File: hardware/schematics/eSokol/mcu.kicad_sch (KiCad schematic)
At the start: 12 parts, among them J1 DB25, Q6 AO3400A, SW1 SW_KEY, U2 YAAJ_BluePill_SWD_Breakout, U3 TP4056, U5 AMS1117-5.0, U8 DS18S20

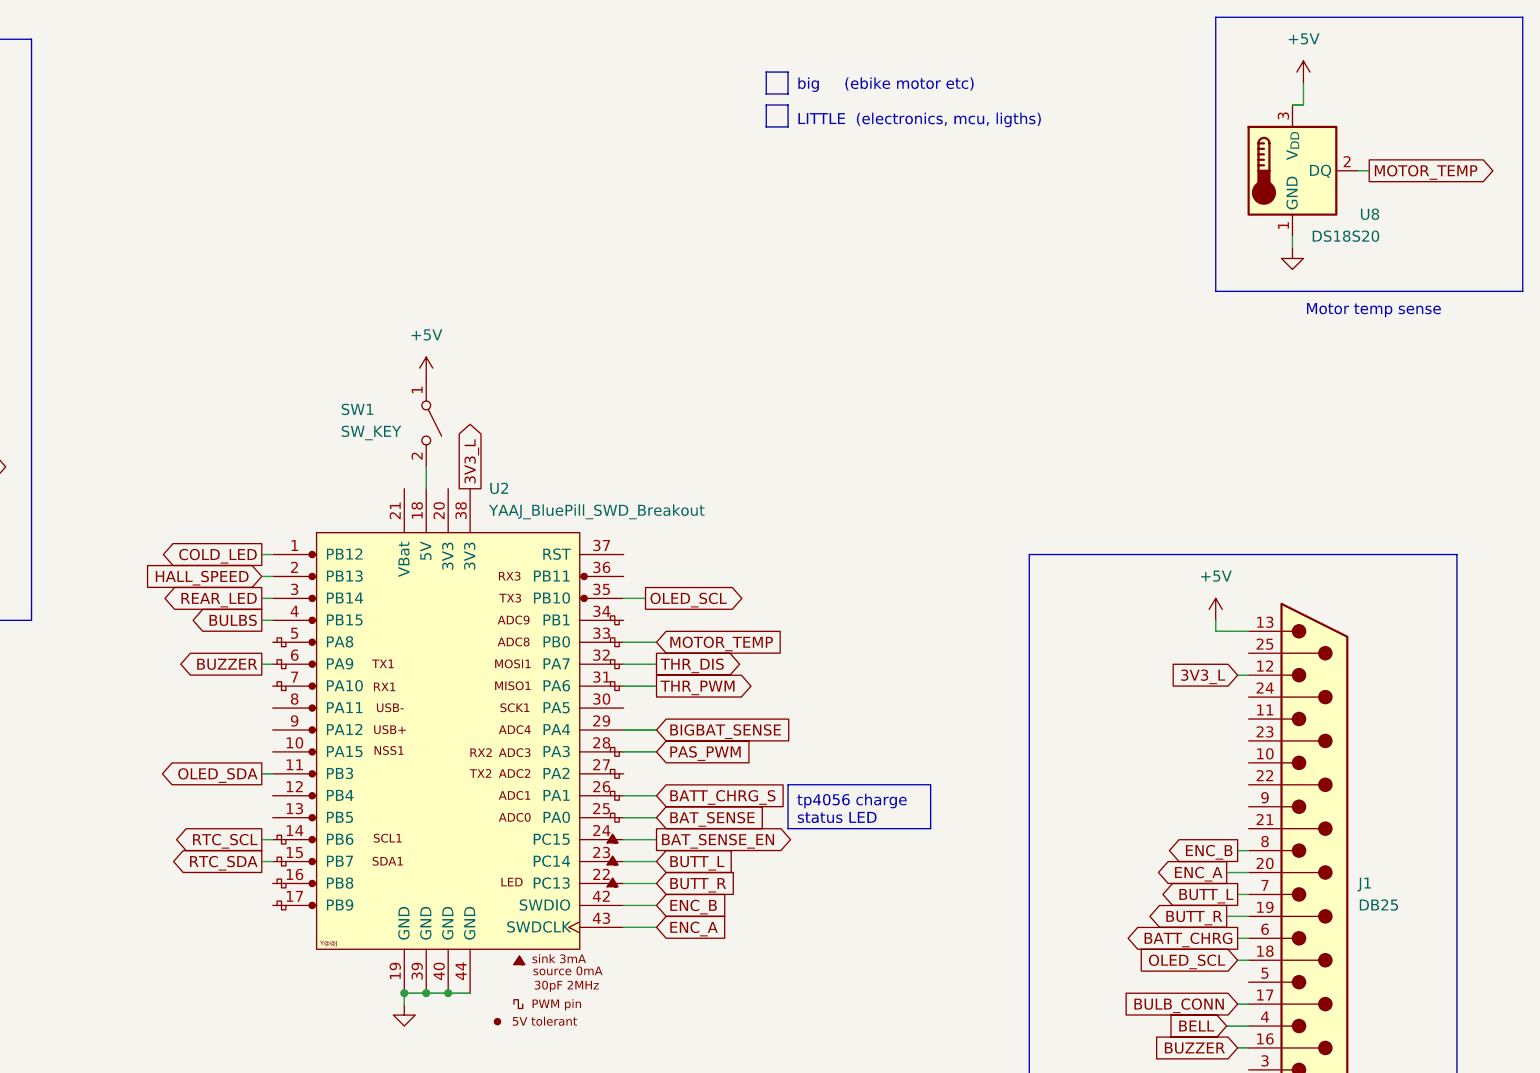
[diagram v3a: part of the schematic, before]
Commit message: Create one BIG schematic containing everything related to motor and its driver
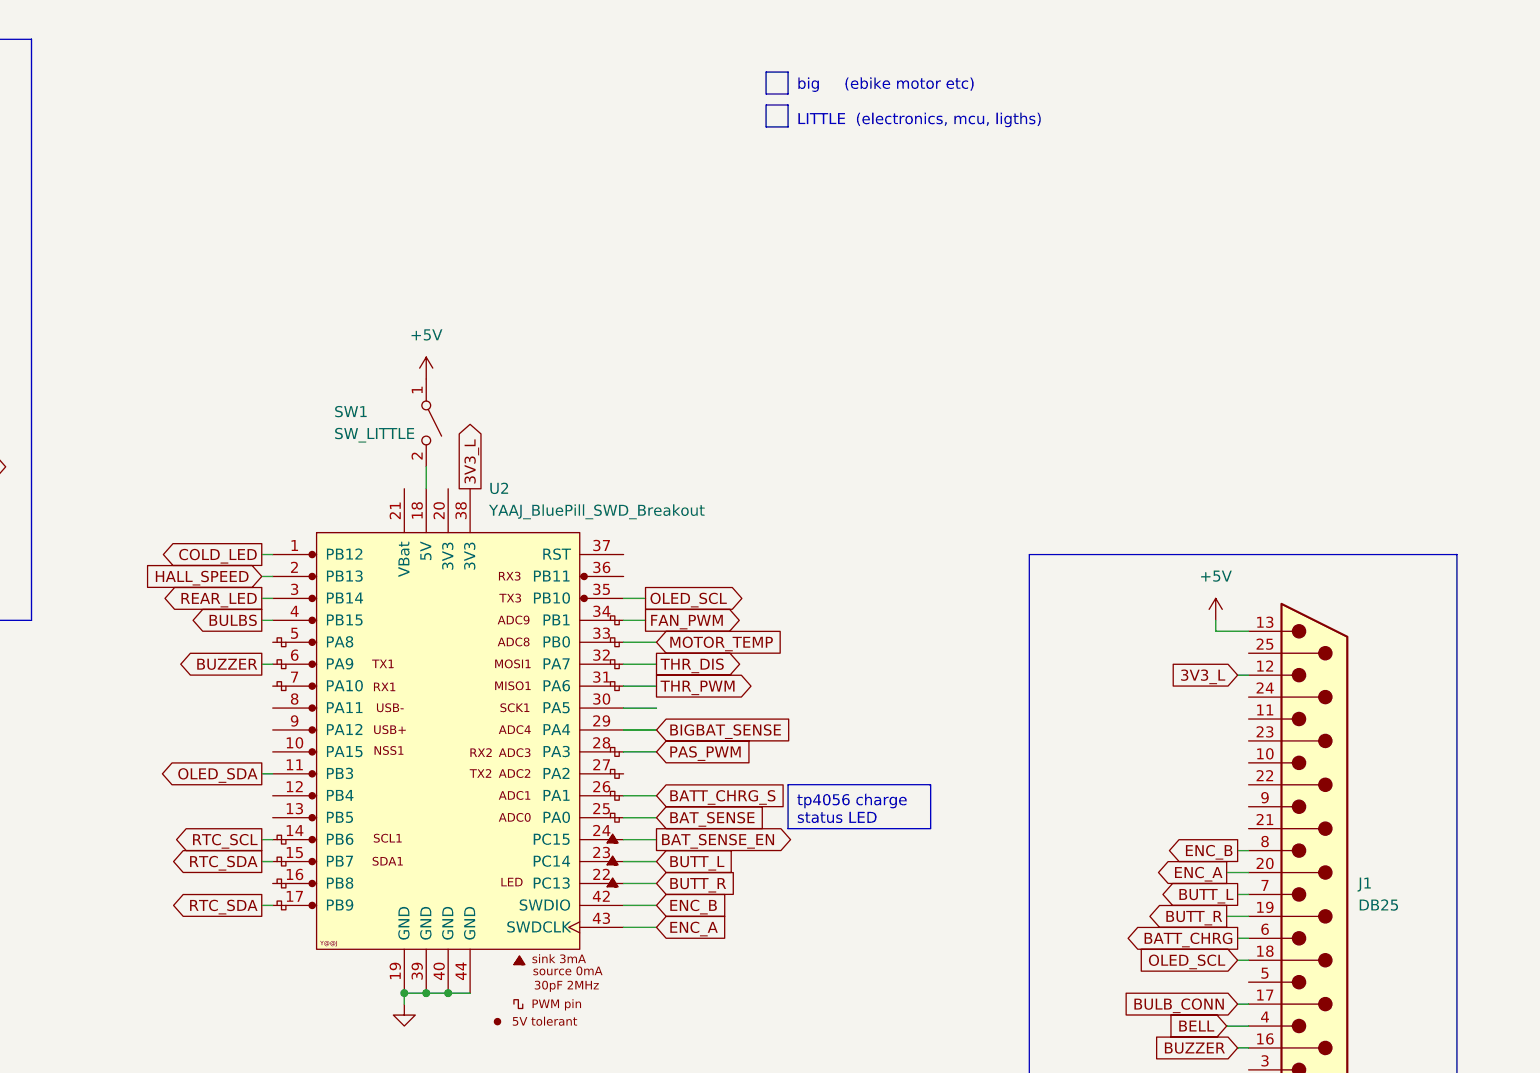
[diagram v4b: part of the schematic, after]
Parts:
- removed U8: DS18S20, Package_TO_SOT_THT:TO-92_Inline, symbol Sensor_Temperature:DS18S20
- SW1: value SW_KEY -> SW_LITTLE
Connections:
- net RTC_SDA: now also U2.17 (PB9)
- net FAN_PWM: now reaches U2.34 (PB1)
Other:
- note removed: "Motor temp sense"
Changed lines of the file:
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@@
+	(wire
+		(pts
+			(xy 177.8 93.98) (xy 181.61 93.98)
+		)
+		(stroke
+			(width 0)
+			(type default)
+		)
+	)
+	(wire
+		(pts
+			(xy 177.8 83.82) (xy 180.34 83.82)
+		)
+		(stroke
+			(width 0)
+			(type default)
+		)
+	)
 	(wire
 		(pts
@@
 	(wire
 		(pts
+			(xy 135.89 116.84) (xy 137.16 116.84)
+		)
+		(stroke
+			(width 0)
+			(type default)
+		)
+	)
+	(wire
+		(pts
 			(xy 135.89 111.76) (xy 137.16 111.76)
 		)
@@
 	(wire
 		(pts
-			(xy 256.54 21.59) (xy 256.54 24.13)
-		)
-		(stroke
-			(width 0)
-			(type default)
-		)
-	)
-	(wire
-		(pts
 			(xy 160.02 182.88) (xy 156.21 182.88)
 		)
@@
 	(wire
 		(pts
-			(xy 255.27 39.37) (xy 255.27 40.64)
-		)
-		(stroke
-			(width 0)
-			(type default)
-		)
-	)
-	(wire
-		(pts
 			(xy 137.16 81.28) (xy 135.89 81.28)
 		)
@@
 	(wire
 		(pts
-			(xy 255.27 24.13) (xy 256.54 24.13)
-		)
-		(stroke
-			(width 0)
-			(type default)
-		)
-	)
-	(wire
-		(pts
 			(xy 250.19 146.05) (xy 250.19 149.86)
 		)
@@
 		(pts
 			(xy 177.8 88.9) (xy 181.61 88.9)
-		)
-		(stroke
-			(width 0)
-			(type default)
-		)
-	)
-	(wire
-		(pts
-			(xy 264.16 31.75) (xy 262.89 31.75)
 		)
 		(stroke
@@
 			(width 0)
 			(type default)
-		)
-		(fill
-			(type none)
-		)
-	)
-	(rectangle
-		(start 246.38 13.97)
-		(end 281.94 45.72)
-		(stroke
-			(width 0)
-			(type default)
-			(color 204 102 0 1)
 		)
 		(fill
@@
 		)
 	)
-	(text "Motor temp sense\n"
-		(exclude_from_sim no)
-		(at 264.668 48.006 0)
-		(effects
-			(font
-				(size 1.27 1.27)
-				(color 204 102 0 1)
-			)
-		)
-	)
 	(text "LPT CONNECTOR (TO BIKE FRONT)"
 		(exclude_from_sim no)
@@
 		)
 	)
+	(global_label "FAN_PWM"
+		(shape output)
+		(at 180.34 83.82 0)
+		(fields_autoplaced yes)
+		(effects
+			(font
+				(size 1.27 1.27)
+				(color 204 102 0 1)
+			)
+			(justify left)
+		)
+		(property "Intersheetrefs" "${INTERSHEET_REFS}"
+			(at 191.9733 83.82 0)
+			(effects
+				(font
+					(size 1.27 1.27)
+				)
+				(justify left)
+				(hide yes)
+			)
+		)
+	)
 	(global_label "BATT_CHRG_S"
 		(shape input)
@@
 		)
 	)
-	(global_label "MOTOR_TEMP"
-		(shape output)
-		(at 264.16 31.75 0)
-		(fields_autoplaced yes)
-		(effects
-			(font
-				(size 1.27 1.27)
-				(color 204 102 0 1)
-			)
-			(justify left)
-		)
-		(property "Intersheetrefs" "${INTERSHEET_REFS}"
-			(at 279.3008 31.75 0)
-			(effects
-				(font
-					(size 1.27 1.27)
-				)
-				(justify left)
-				(hide yes)
-			)
-		)
-	)
 	(global_label "RTC_SDA"
 		(shape output)
@@
 		(property "Intersheetrefs" "${INTERSHEET_REFS}"
 			(at 238.8591 113.03 0)
+			(effects
+				(font
+					(size 1.27 1.27)
+				)
+				(justify right)
+				(hide yes)
+			)
+		)
+	)
+	(global_label "RTC_SDA"
+		(shape output)
+		(at 135.89 116.84 180)
+		(fields_autoplaced yes)
+		(effects
+			(font
+				(size 1.27 1.27)
+			)
+			(justify right)
+		)
+		(property "Intersheetrefs" "${INTERSHEET_REFS}"
+			(at 124.8615 116.84 0)
 			(effects
 				(font
@@
 	)
 	(symbol
-		(lib_id "power:+5V")
-		(at 256.54 21.59 0)
-		(unit 1)
-		(exclude_from_sim no)
-		(in_bom yes)
-		(on_board yes)
-		(dnp no)
-		(fields_autoplaced yes)
-		(property "Reference" "#PWR062"
-			(at 256.54 25.4 0)
-			(effects
-				(font
-					(size 1.27 1.27)
-				)
-				(hide yes)
-			)
-		)
-		(property "Value" "+5V"
-			(at 256.54 16.51 0)
-			(effects
-				(font
-					(size 1.27 1.27)
-				)
-			)
-		)
-		(property "Footprint" ""
-			(at 256.54 21.59 0)
-			(effects
-				(font
-					(size 1.27 1.27)
-				)
-				(hide yes)
-			)
-		)
-		(property "Datasheet" ""
-			(at 256.54 21.59 0)
-			(effects
-				(font
-					(size 1.27 1.27)
-				)
-				(hide yes)
-			)
-		)
-		(property "Description" "Power symbol creates a global label with name \"+5V\""
-			(at 256.54 21.59 0)
-			(effects
-				(font
-					(size 1.27 1.27)
-				)
-				(hide yes)
-			)
-		)
-		(pin "1"
-		)
-		(instances
-			(project "eSokol"
-				(path "/44b9e6ec-08e4-4361-b4b8-e7c9cf0a26a7/f565501d-a817-4ef9-831d-033eb352bbe6"
-					(reference "#PWR062")
-					(unit 1)
-				)
-			)
-		)
-	)
-	(symbol
 		(lib_id "power:+BATT")
 		(at 26.67 64.77 90)
@@
 		(dnp no)
 		(property "Reference" "SW1"
-			(at 145.034 59.436 90)
-			(effects
-				(font
-					(size 1.27 1.27)
-				)
-				(justify left)
-			)
-		)
-		(property "Value" "SW_KEY"
-			(at 145.034 61.976 90)
+			(at 144.272 59.69 90)
+			(effects
+				(font
+					(size 1.27 1.27)
+				)
+				(justify left)
+			)
+		)
+		(property "Value" "SW_LITTLE"
+			(at 144.272 62.23 90)
 			(effects
 				(font
@@
 				(path "/44b9e6ec-08e4-4361-b4b8-e7c9cf0a26a7/f565501d-a817-4ef9-831d-033eb352bbe6"
 					(reference "SW1")
-					(unit 1)
-				)
-			)
-		)
-	)
-	(symbol
-		(lib_id "power:GND")
-		(at 255.27 40.64 0)
-		(unit 1)
-		(exclude_from_sim no)
-		(in_bom yes)
-		(on_board yes)
-		(dnp no)
-		(fields_autoplaced yes)
-		(property "Reference" "#PWR063"
-			(at 255.27 46.99 0)
-			(effects
-				(font
-					(size 1.27 1.27)
-				)
-				(hide yes)
-			)
-		)
-		(property "Value" "GND"
-			(at 255.27 45.72 0)
-			(effects
-				(font
-					(size 1.27 1.27)
-				)
-				(hide yes)
-			)
-		)
-		(property "Footprint" ""
-			(at 255.27 40.64 0)
-			(effects
-				(font
-					(size 1.27 1.27)
-				)
-				(hide yes)
-			)
-		)
-		(property "Datasheet" ""
-			(at 255.27 40.64 0)
-			(effects
-				(font
-					(size 1.27 1.27)
-				)
-				(hide yes)
-			)
-		)
-		(property "Description" "Power symbol creates a global label with name \"GND\" , ground"
-			(at 255.27 40.64 0)
-			(effects
-				(font
-					(size 1.27 1.27)
-				)
-				(hide yes)
-			)
-		)
-		(pin "1"
-		)
-		(instances
-			(project "eSokol"
-				(path "/44b9e6ec-08e4-4361-b4b8-e7c9cf0a26a7/f565501d-a817-4ef9-831d-033eb352bbe6"
-					(reference "#PWR063")
 					(unit 1)
 				)
@@
 					(unit 1)
 				)
-			)
-		)
-	)
-	(symbol
-		(lib_id "Sensor_Temperature:DS18S20")
-		(at 255.27 31.75 0)
-		(unit 1)
-		(exclude_from_sim no)
-		(in_bom yes)
-		(on_board yes)
-		(dnp no)
-		(property "Reference" "U8"
-			(at 265.43 36.83 0)
-			(effects
-				(font
-					(size 1.27 1.27)
-				)
-				(justify right)
-			)
-		)
-		(property "Value" "DS18S20"
-			(at 265.43 39.37 0)
-			(effects
-				(font
-					(size 1.27 1.27)
-				)
-				(justify right)
-			)
-		)
-		(property "Footprint" "Package_TO_SOT_THT:TO-92_Inline"
-			(at 229.87 38.1 0)
-			(effects
-				(font
-					(size 1.27 1.27)
-				)
-				(hide yes)
-			)
-		)
-		(property "Datasheet" "http://datasheets.maximintegrated.com/en/ds/DS18S20.pdf"
-			(at 251.46 25.4 0)
-			(effects
-				(font
-					(size 1.27 1.27)
-				)
-				(hide yes)
-			)
-		)
-		(property "Description" "High-Precision 1-Wire Digital Thermometer TO-92"
-			(at 255.27 31.75 0)
-			(effects
-				(font
-					(size 1.27 1.27)
-				)
-				(hide yes)
-			)
-		)
-		(pin "3"
-		)
-		(pin "2"
-		)
-		(pin "1"
-		)
-		(instances
-			(project ""
-				(path "/44b9e6ec-08e4-4361-b4b8-e7c9cf0a26a7/f565501d-a817-4ef9-831d-033eb352bbe6"
-					(reference "U8")
-					(unit 1)
-				)

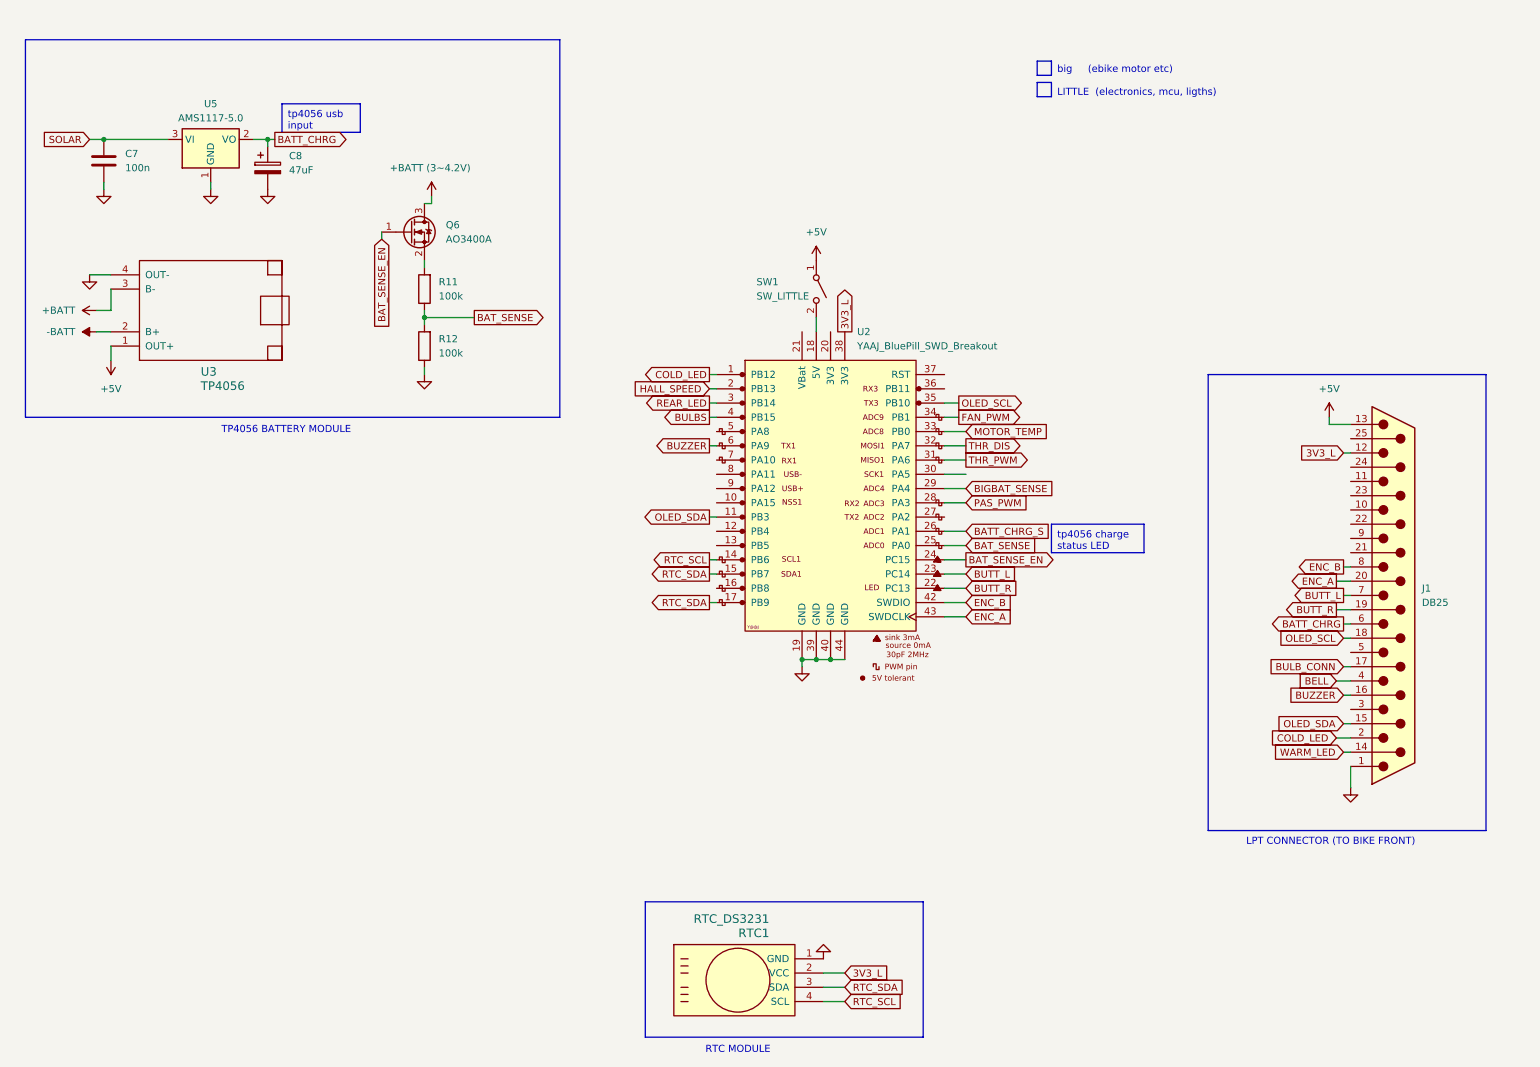
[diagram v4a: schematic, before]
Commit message: Initial TCRT5000-based rider detect, rearrange MCU pin layout
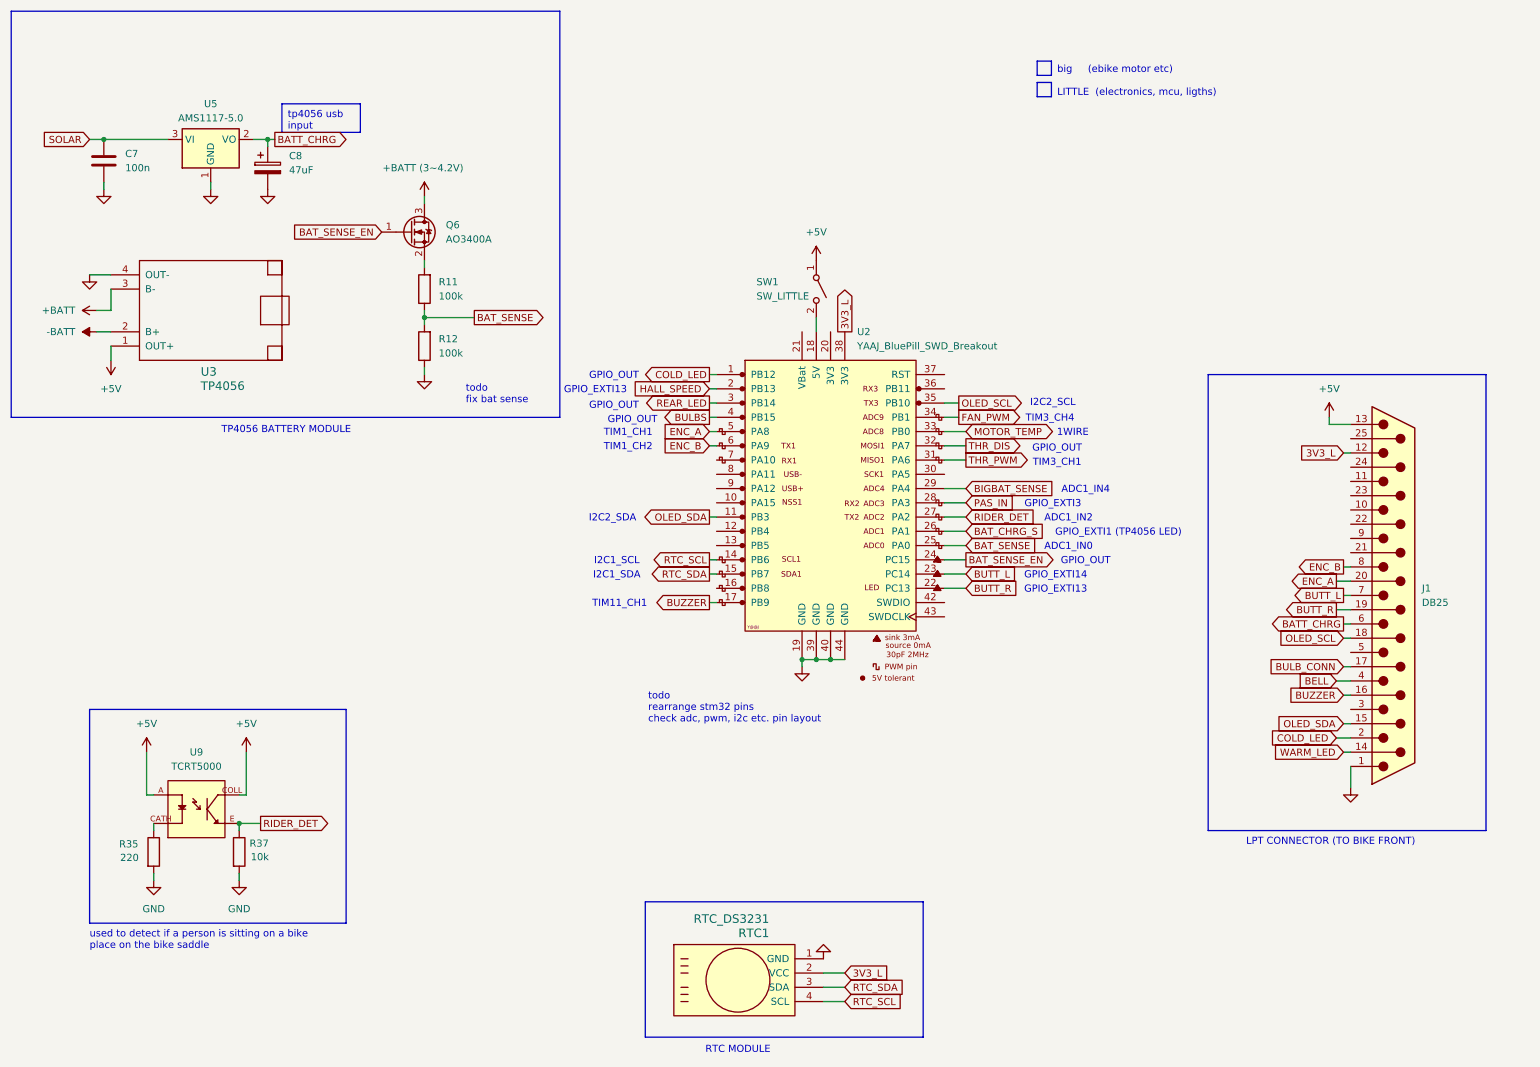
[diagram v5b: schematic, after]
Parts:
- added R35: 220, symbol Device:R
- added R37: 10k, symbol Device:R
- added U9: TCRT5000, TCRT5000:OPTO_TCRT5000, symbol TCRT5000:TCRT5000
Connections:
- net +5V: now also U9.A, U9.COLL
- net BUZZER: now also U2.17 (PB9); no longer U2.6 (PA9)
- net ENC_A: now also U2.5 (PA8); no longer U2.43 (SWDCLK)
- net ENC_B: now also U2.6 (PA9); no longer U2.42 (SWDIO)
- net GND: now also R35.2, R37.2
- net RTC_SDA: no longer U2.17 (PB9)
- net RIDER_DET: now reaches U2.27 (PA2)
- net RIDER_DET: now also R37.1, U9.E
- net BATT_CHRG_S renamed BAT_CHRG_S
- net PAS_PWM renamed PAS_IN
- new net: R35.1, U9.CATH
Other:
- note added: "1WIRE"
- note added: "ADC1_IN0"
- note added: "ADC1_IN2"
- note added: "ADC1_IN4"
- note added: "GPIO_EXTI1 (TP4056 LED)"
- note added: "GPIO_EXTI13"
- note added: "GPIO_EXTI14"
- note added: "GPIO_EXTI3"
- note added: "GPIO_OUT"
- note added: "I2C1_SCL"
- note added: "I2C1_SDA"
- note added: "I2C2_SCL"
- note added: "I2C2_SDA"
- note added: "TIM11_CH1"
- note added: "TIM1_CH1"
- note added: "TIM1_CH2"
- note added: "TIM3_CH1"
- note added: "TIM3_CH4"
- note added: "todo fix bat sense"
- note added: "todo rearrange stm32 pins check adc, pwm, i2c etc. pin layout"
- note added: "used to detect if a person is sitting on a bike place on the bike saddle"
